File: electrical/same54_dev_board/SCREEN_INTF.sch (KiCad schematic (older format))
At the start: 4 parts, among them J3 Conn_02x20_Odd_Even_LCD_INTF, U3 MAX7301AAX+

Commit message: Trying to figure out how I want to do power...
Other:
- note added: "LCD Interface"
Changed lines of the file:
@@
 	10850 2500 10850 2650
 $Comp
-L power:GND #PWR?
+L power:GND #PWR0109
 U 1 1 5EC6B772
 P 10850 2650
-F 0 "#PWR?" H 10850 2400 50  0001 C CNN
+F 0 "#PWR0109" H 10850 2400 50  0001 C CNN
 F 1 "GND" H 10855 2477 50  0000 C CNN
 F 2 "" H 10850 2650 50  0001 C CNN
@@
 Wire Bus Line
 	8200 4050 8450 4050
+Entry Bus Bus
+	8900 3750 9000 3650
+Wire Notes Line
+	550  550  1350 550
+Wire Notes Line
+	1350 550  1350 1200
+Wire Notes Line
+	1350 1200 550  1200
+Wire Notes Line
+	550  1200 550  550
+Wire Notes Line
+	550  1250 550  3000
+Wire Notes Line
+	550  3000 2200 3000
+Wire Notes Line
+	2200 3000 2200 1250
+Wire Notes Line
+	2200 1250 550  1250
 Wire Bus Line
 	9050 3650 9050 4750
@@
 Wire Bus Line
 	10900 3650 10900 5600
-Entry Bus Bus
-	8900 3750 9000 3650
+Text Notes 650  1350 0    50   ~ 0
+LCD Interface
 $EndSCHEMATC

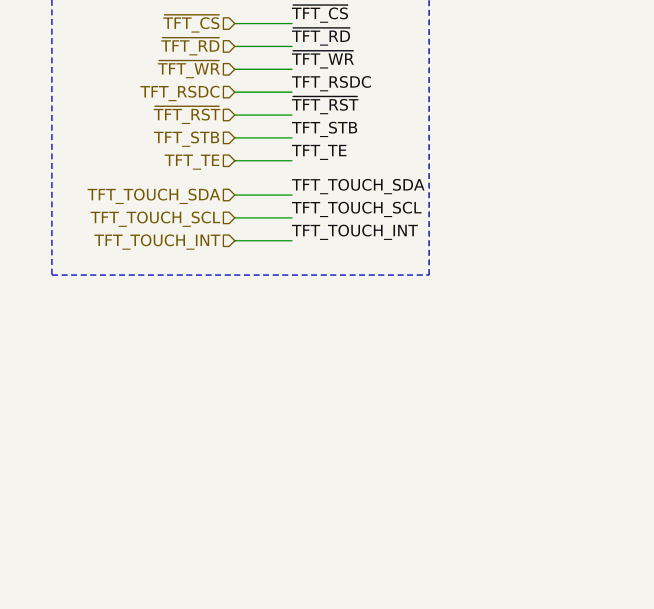
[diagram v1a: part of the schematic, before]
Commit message: Added usart, i2c, and spi pin locations, as well as labeled sercoms
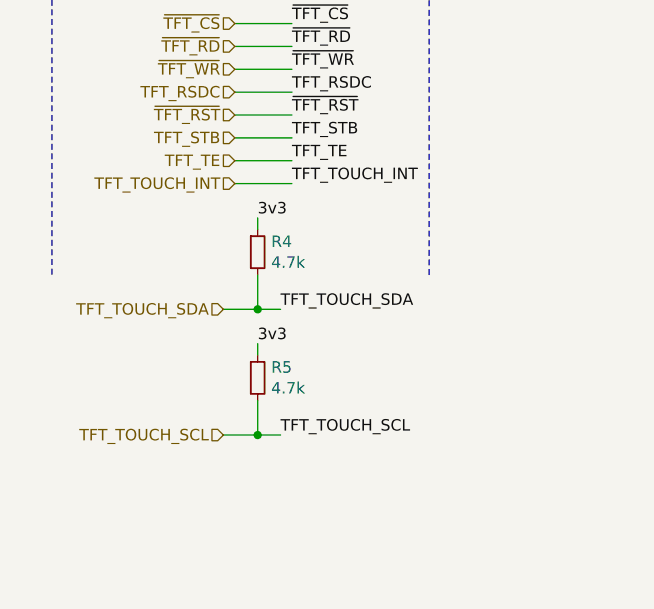
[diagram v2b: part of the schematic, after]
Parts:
- added R4, R5: 4.7k, symbol Device:R_Small
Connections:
- net TFT_TOUCH_SCL: now also R5.2
- net TFT_TOUCH_SDA: now also R4.2
- net g_3v3: now also R4.1, R5.1
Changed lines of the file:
@@
 Text HLabel 1350 2400 0    50   Input ~ 0
 TFT_STB
-Text HLabel 1350 2650 0    50   Input ~ 0
+Text HLabel 1300 3150 0    50   Input ~ 0
 TFT_TOUCH_SDA
-Text HLabel 1350 2750 0    50   Input ~ 0
+Text HLabel 1300 3700 0    50   Input ~ 0
 TFT_TOUCH_SCL
-Text HLabel 1350 2850 0    50   Input ~ 0
+Text HLabel 1350 2600 0    50   Input ~ 0
 TFT_TOUCH_INT
 Entry Bus Bus
@@
 Wire Wire Line
 	1600 2400 1350 2400
-Text Label 1600 2650 0    50   ~ 0
+Text Label 1550 3150 0    50   ~ 0
 TFT_TOUCH_SDA
 Wire Wire Line
-	1600 2650 1350 2650
-Wire Wire Line
-	1350 2750 1600 2750
-Text Label 1600 2750 0    50   ~ 0
+	1300 3700 1450 3700
+Text Label 1550 3700 0    50   ~ 0
 TFT_TOUCH_SCL
-Text Label 1600 2850 0    50   ~ 0
+Text Label 1600 2600 0    50   ~ 0
 TFT_TOUCH_INT
 Wire Wire Line
-	1600 2850 1350 2850
+	1600 2600 1350 2600
 Wire Wire Line
 	7900 3650 8000 3650
@@
 	550  1250 550  3000
 Wire Notes Line
-	550  3000 2200 3000
-Wire Notes Line
 	2200 3000 2200 1250
 Wire Notes Line
 	2200 1250 550  1250
-Wire Bus Line
-	9050 3650 9050 4750
-Wire Bus Line
-	8200 4050 8200 6200
-Wire Bus Line
-	6300 4050 6300 6200
-Wire Bus Line
-	10900 3650 10900 5600
 Text Notes 650  1350 0    50   ~ 0
 LCD Interface
+Connection ~ 1450 3150
+Wire Wire Line
+	1450 3150 1300 3150
+Wire Wire Line
+	1550 3150 1450 3150
+Text Label 1450 2750 0    50   ~ 0
+3v3
+Wire Wire Line
+	1450 2800 1450 2750
+$Comp
+L Device:R_Small R4
+U 1 1 5E833EF1
+P 1450 2900
+F 0 "R4" H 1509 2946 50  0000 L CNN
+F 1 "4.7k" H 1509 2855 50  0000 L CNN
+F 2 "" H 1450 2900 50  0001 C CNN
+F 3 "~" H 1450 2900 50  0001 C CNN
+	1    1450 2900
+	1    0    0    -1
+$EndComp
+Wire Wire Line
+	1450 3150 1450 3000
+Text Label 1450 3300 0    50   ~ 0
+3v3
+Wire Wire Line
+	1450 3350 1450 3300
+$Comp
+L Device:R_Small R5
+U 1 1 5E84B2E4
+P 1450 3450
+F 0 "R5" H 1509 3496 50  0000 L CNN
+F 1 "4.7k" H 1509 3405 50  0000 L CNN
+F 2 "" H 1450 3450 50  0001 C CNN
+F 3 "~" H 1450 3450 50  0001 C CNN
+	1    1450 3450
+	1    0    0    -1
+$EndComp
+Wire Wire Line
+	1450 3700 1450 3550
+Connection ~ 1450 3700
+Wire Wire Line
+	1450 3700 1550 3700
+Wire Bus Line
+	9050 3650 9050 4750
+Wire Bus Line
+	8200 4050 8200 6200
+Wire Bus Line
+	6300 4050 6300 6200
+Wire Bus Line
+	10900 3650 10900 5600
 $EndSCHEMATC

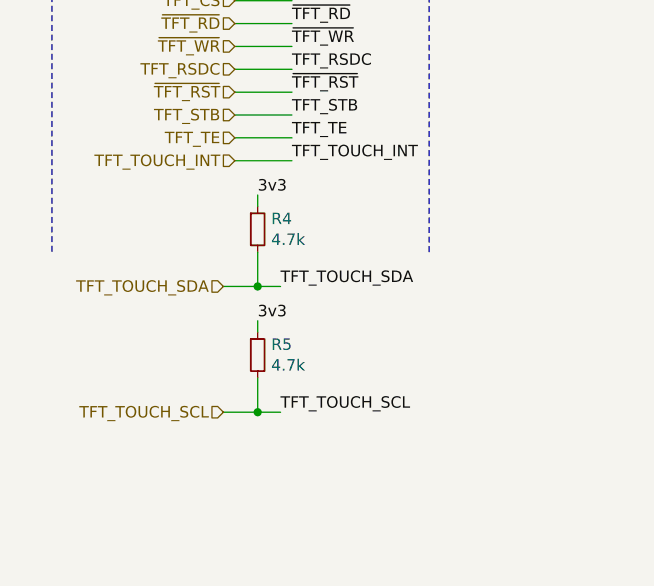
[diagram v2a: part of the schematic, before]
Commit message: Made board smaller, changed some small things
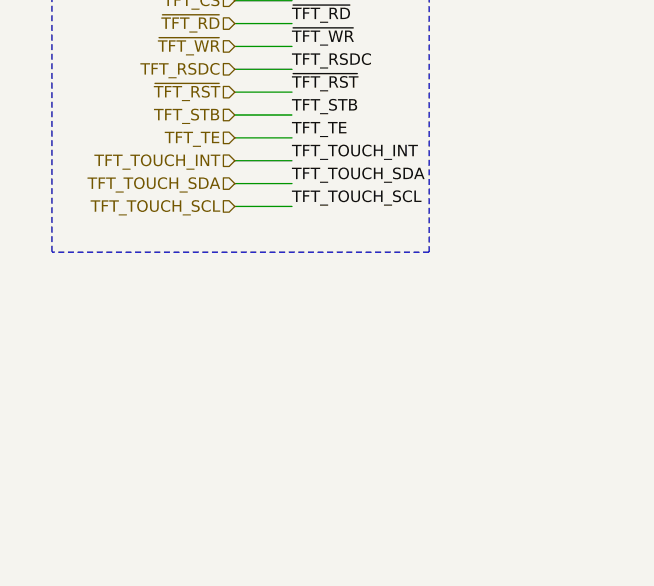
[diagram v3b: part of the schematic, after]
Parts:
- removed R4, R5: 4.7k, symbol Device:R_Small
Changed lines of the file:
@@
 $Descr A4 11693 8268
 encoding utf-8
-Sheet 5 5
+Sheet 3 5
 Title ""
 Date ""
@@
 Text HLabel 1350 2400 0    50   Input ~ 0
 TFT_STB
-Text HLabel 1300 3150 0    50   Input ~ 0
+Text HLabel 1350 2700 0    50   Input ~ 0
 TFT_TOUCH_SDA
-Text HLabel 1300 3700 0    50   Input ~ 0
+Text HLabel 1350 2800 0    50   Input ~ 0
 TFT_TOUCH_SCL
 Text HLabel 1350 2600 0    50   Input ~ 0
@@
 Wire Wire Line
 	1600 2400 1350 2400
-Text Label 1550 3150 0    50   ~ 0
-TFT_TOUCH_SDA
-Wire Wire Line
-	1300 3700 1450 3700
-Text Label 1550 3700 0    50   ~ 0
+Text Label 1600 2800 0    50   ~ 0
 TFT_TOUCH_SCL
 Text Label 1600 2600 0    50   ~ 0
@@
 Text Notes 650  1350 0    50   ~ 0
 LCD Interface
-Connection ~ 1450 3150
-Wire Wire Line
-	1450 3150 1300 3150
-Wire Wire Line
-	1550 3150 1450 3150
-Text Label 1450 2750 0    50   ~ 0
-3v3
-Wire Wire Line
-	1450 2800 1450 2750
-$Comp
-L Device:R_Small R4
-U 1 1 5E833EF1
-P 1450 2900
-F 0 "R4" H 1509 2946 50  0000 L CNN
-F 1 "4.7k" H 1509 2855 50  0000 L CNN
-F 2 "" H 1450 2900 50  0001 C CNN
-F 3 "~" H 1450 2900 50  0001 C CNN
-	1    1450 2900
-	1    0    0    -1
-$EndComp
-Wire Wire Line
-	1450 3150 1450 3000
-Text Label 1450 3300 0    50   ~ 0
-3v3
-Wire Wire Line
-	1450 3350 1450 3300
-$Comp
-L Device:R_Small R5
-U 1 1 5E84B2E4
-P 1450 3450
-F 0 "R5" H 1509 3496 50  0000 L CNN
-F 1 "4.7k" H 1509 3405 50  0000 L CNN
-F 2 "" H 1450 3450 50  0001 C CNN
-F 3 "~" H 1450 3450 50  0001 C CNN
-	1    1450 3450
-	1    0    0    -1
-$EndComp
-Wire Wire Line
-	1450 3700 1450 3550
-Connection ~ 1450 3700
-Wire Wire Line
-	1450 3700 1550 3700
+Text Label 1600 2700 0    50   ~ 0
+TFT_TOUCH_SDA
+Wire Wire Line
+	1350 2700 1600 2700
+Wire Wire Line
+	1350 2800 1600 2800
+Wire Notes Line
+	2200 3000 550  3000
 Wire Bus Line
 	9050 3650 9050 4750
